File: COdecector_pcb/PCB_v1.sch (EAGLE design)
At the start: 31 parts, among them IC2 FT230XS, X1 MINI-USB-32005-301

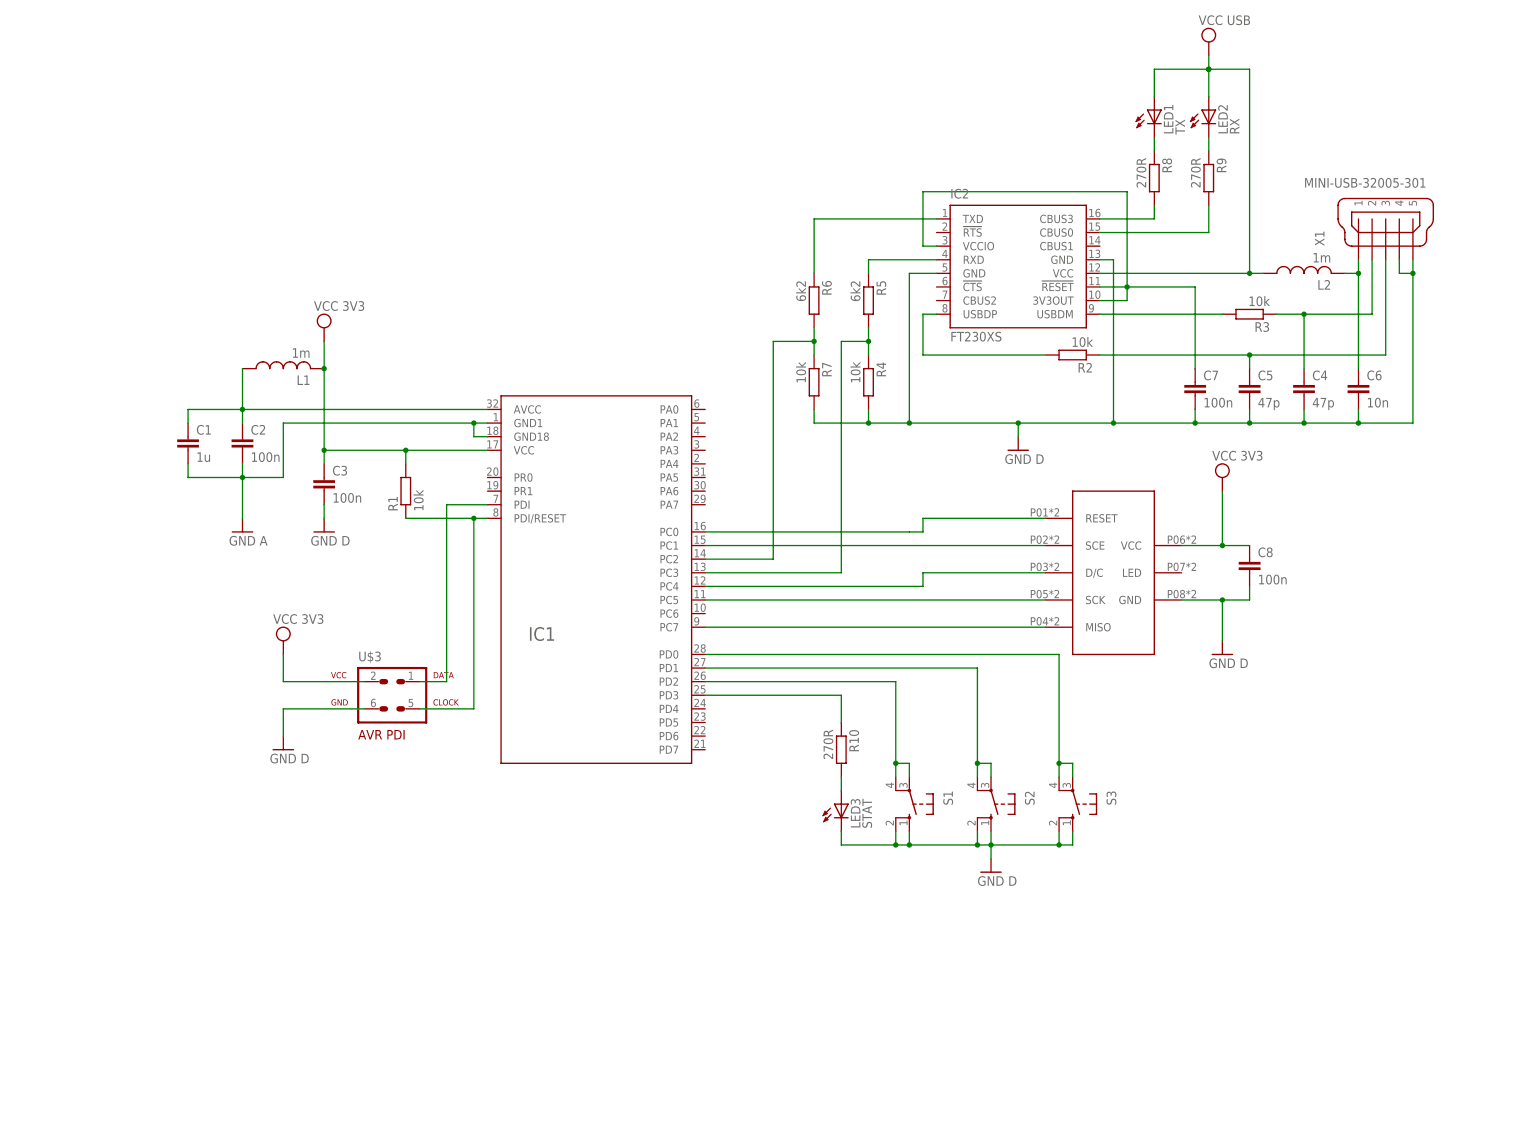
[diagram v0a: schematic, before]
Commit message: Added Vbat divider
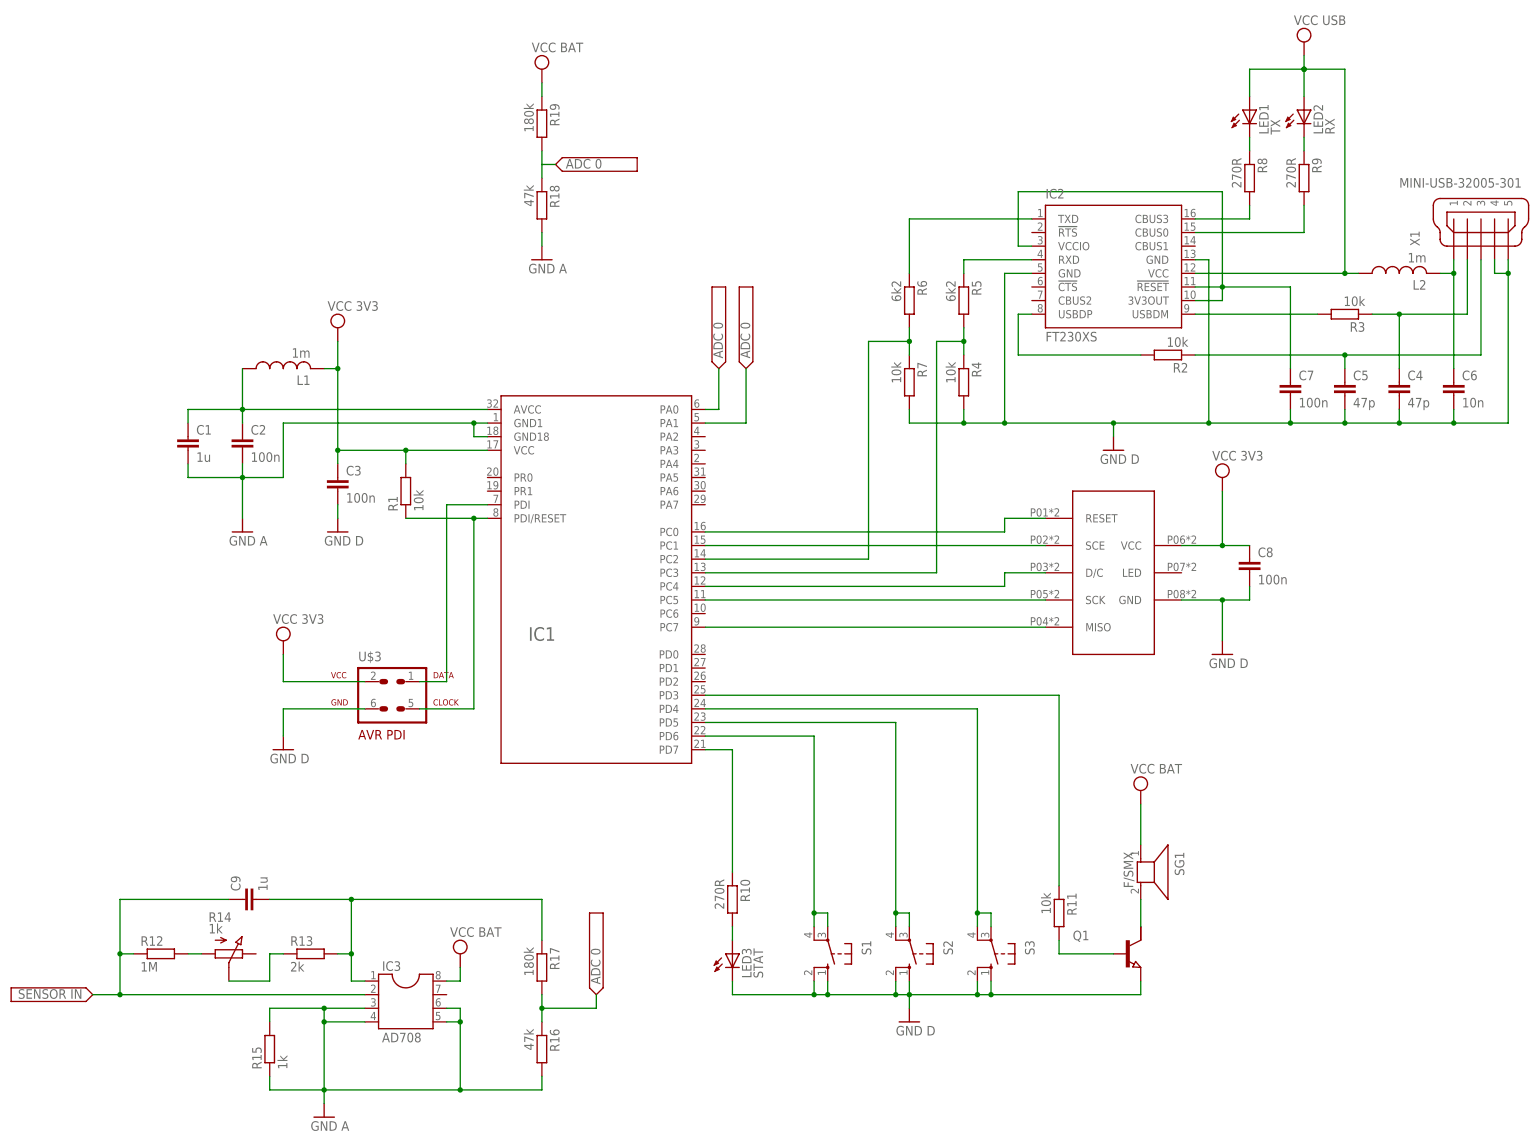
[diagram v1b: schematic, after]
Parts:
- added C9: 1u, eagle-ltspice:C
- added IC3: AD708, ic-package:DIL8
- added Q1: (no value), semicon-smd-ipc:NPN-TRANSISTIOR-2COLSOT143
- added R11: 10k, eagle-ltspice:RR3216
- added R12: 1M, eagle-ltspice:RR3216
- added R13: 2k, eagle-ltspice:RR3216
- added R14: 1k, pot-vitrohm:PC25
- added R15: 1k, eagle-ltspice:RR3216
- added R16, R18: 47k, eagle-ltspice:RR3216
- added R17, R19: 180k, eagle-ltspice:RR3216
- added SG1: F/SMX, buzzer:F/SMX
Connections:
- new net N$28: Q1.C, SG1.2
- new net N$29: R12.2, R14.A
- new net N$30: Q1.B, R11.2
- new net N$31: IC1.PD3, R11.1
- new net N$32: IC1.PA0
- new net N$33: R13.1, R14.S
- new net N$34: C9.2, IC3.1, R13.2, R17.1
- new net N$35: C9.1, IC3.2, R12.1
- new net N$36: R16.1, R17.2
- new net N$37: IC1.PA1
- new net N$39: R18.1, R19.2
- net GND: now also IC3.3, IC3.4, IC3.5, IC3.6, Q1.E, R15.1, R15.2, R16.2, R18.2
- net N$24: now also IC1.PD5; no longer IC1.PD1
- net N$25: now also IC1.PD6; no longer IC1.PD2
- net N$27: now also IC1.PD7; no longer IC1.PD3
- net N$7: now also IC1.PD4; no longer IC1.PD0
- net VCC: now also IC3.8, R19.1, SG1.1
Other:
- moved on the sheet: C3, C4, C5, C6, C7, IC2, L2, LED1, LED2, LED3, R10, R2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

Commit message: Start with layout
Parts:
- removed R4: 10k, eagle-ltspice:RR3216
- removed R5: 6k2, eagle-ltspice:RR3216
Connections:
- removed net N$18: IC2.RXD, R5.1
- net GND: no longer R4.2
- net N$19: now also IC2.RXD; no longer R4.1, R5.2
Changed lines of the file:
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@@
 <part name="L2" library="rcl" deviceset="L-US" device="L2012C" value="1m"/>
 <part name="SUPPLY4" library="supply2" deviceset="VCC" device="" value="VCC USB"/>
-<part name="R4" library="eagle-ltspice" deviceset="R" device="R3216" value="10k"/>
-<part name="R5" library="eagle-ltspice" deviceset="R" device="R3216" value="6k2"/>
 <part name="R6" library="eagle-ltspice" deviceset="R" device="R3216" value="6k2"/>
 <part name="R7" library="eagle-ltspice" deviceset="R" device="R3216" value="10k"/>
@@
 <instance part="L2" gate="G$1" x="226.06" y="134.62" rot="R90"/>
 <instance part="SUPPLY4" gate="G$1" x="208.28" y="177.8"/>
-<instance part="R4" gate="G$1" x="144.78" y="114.3" rot="R270"/>
-<instance part="R5" gate="G$1" x="144.78" y="129.54" rot="R270"/>
 <instance part="R6" gate="G$1" x="134.62" y="129.54" rot="R270"/>
 <instance part="R7" gate="G$1" x="134.62" y="114.3" rot="R270"/>
@@
 <pinref part="R7" gate="G$1" pin="2"/>
 <wire x1="134.62" y1="109.22" x2="134.62" y2="106.68" width="0.1524" layer="91"/>
-<pinref part="R4" gate="G$1" pin="2"/>
-<wire x1="134.62" y1="106.68" x2="144.78" y2="106.68" width="0.1524" layer="91"/>
-<wire x1="144.78" y1="106.68" x2="144.78" y2="109.22" width="0.1524" layer="91"/>
-<wire x1="144.78" y1="106.68" x2="152.4" y2="106.68" width="0.1524" layer="91"/>
-<junction x="144.78" y="106.68"/>
+<wire x1="134.62" y1="106.68" x2="152.4" y2="106.68" width="0.1524" layer="91"/>
 <junction x="152.4" y="106.68"/>
 <pinref part="C7" gate="G$1" pin="2"/>
@@
 </segment>
 </net>
-<net name="N$18" class="0">
-<segment>
-<pinref part="IC2" gate="G$1" pin="RXD"/>
-<wire x1="157.48" y1="137.16" x2="144.78" y2="137.16" width="0.1524" layer="91"/>
-<pinref part="R5" gate="G$1" pin="1"/>
-<wire x1="144.78" y1="134.62" x2="144.78" y2="137.16" width="0.1524" layer="91"/>
-</segment>
-</net>
 <net name="N$17" class="0">
 <segment>
@@
 <net name="N$19" class="0">
 <segment>
-<pinref part="R4" gate="G$1" pin="1"/>
-<pinref part="R5" gate="G$1" pin="2"/>
-<wire x1="144.78" y1="119.38" x2="144.78" y2="121.92" width="0.1524" layer="91"/>
 <pinref part="IC1" gate="G$1" pin="PC3"/>
-<wire x1="144.78" y1="121.92" x2="144.78" y2="124.46" width="0.1524" layer="91"/>
-<wire x1="139.7" y1="78.74" x2="96.52" y2="78.74" width="0.1524" layer="91"/>
-<wire x1="144.78" y1="121.92" x2="139.7" y2="121.92" width="0.1524" layer="91"/>
-<wire x1="139.7" y1="121.92" x2="139.7" y2="78.74" width="0.1524" layer="91"/>
-<junction x="144.78" y="121.92"/>
-</segment>
-</net>
+<wire x1="144.78" y1="78.74" x2="96.52" y2="78.74" width="0.1524" layer="91"/>
+<pinref part="IC2" gate="G$1" pin="RXD"/>
+<wire x1="157.48" y1="137.16" x2="147.32" y2="137.16" width="0.1524" layer="91"/>
+<wire x1="144.78" y1="78.74" x2="144.78" y2="137.16" width="0.1524" layer="91"/>
+<wire x1="144.78" y1="137.16" x2="147.32" y2="137.16" width="0.1524" layer="91"/>
+</segment>
+</net>
